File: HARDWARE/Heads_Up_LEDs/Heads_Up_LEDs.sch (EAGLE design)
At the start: 4 parts, among them J1 AUDIO_JACK_TRRSSMD_RA

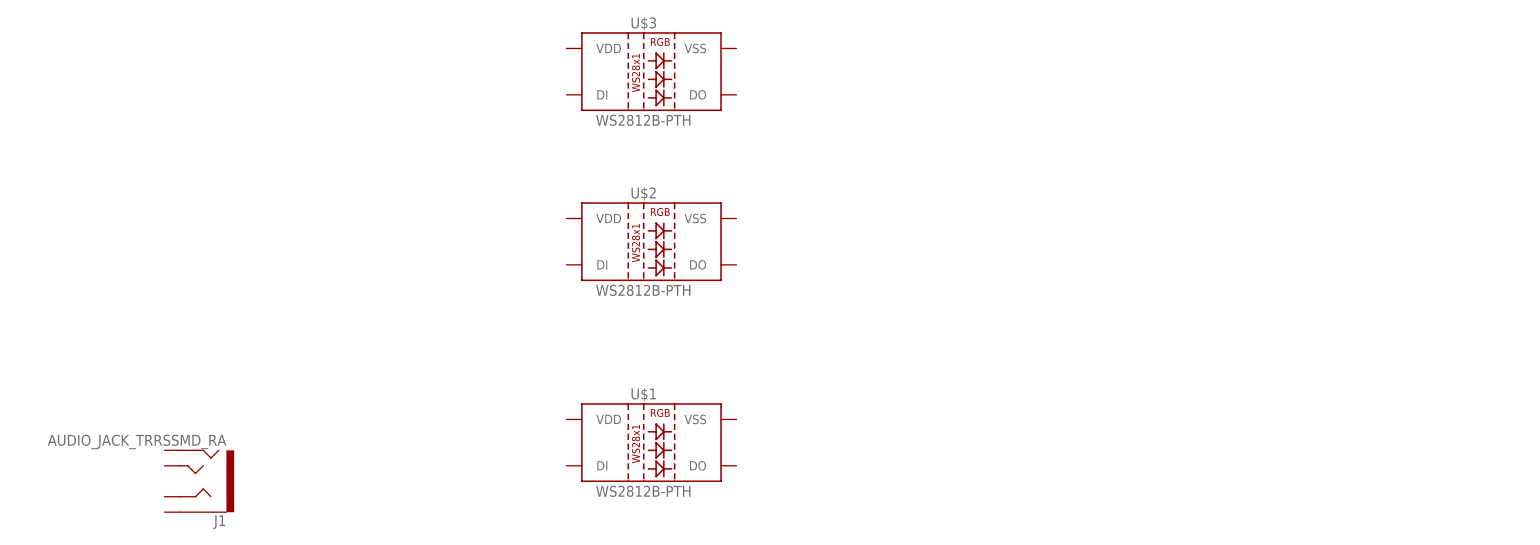
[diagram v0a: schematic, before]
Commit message: heads up leds with ws2812s - v01
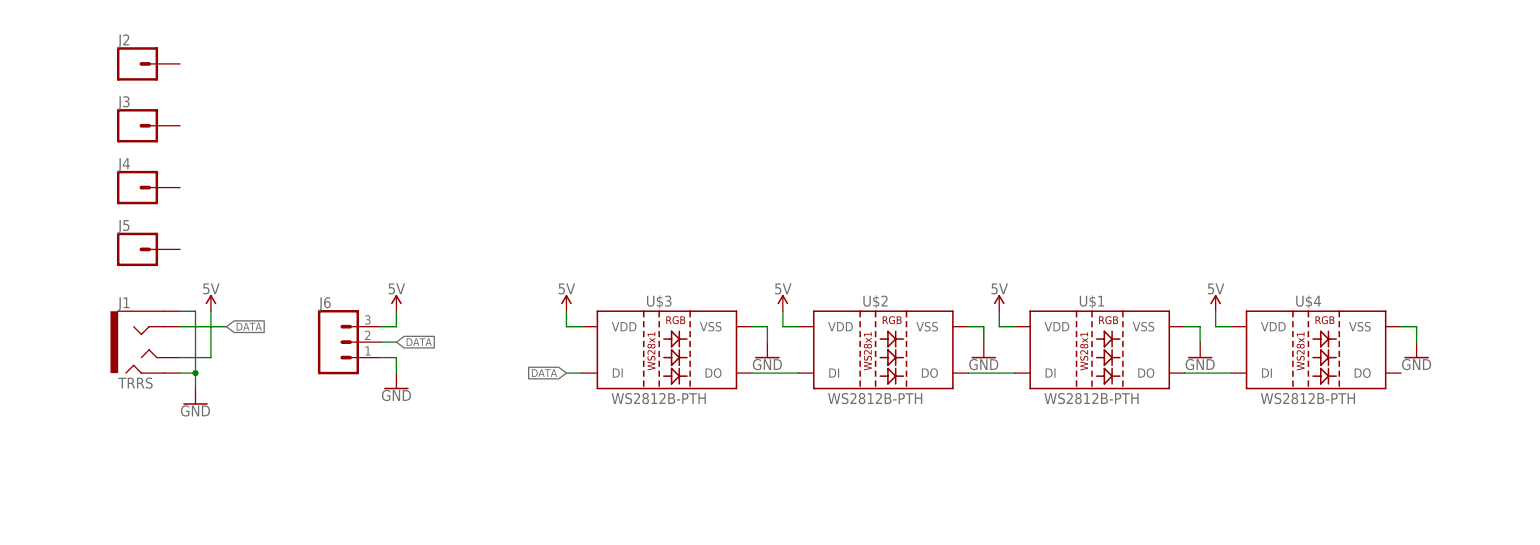
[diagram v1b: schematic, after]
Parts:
- added J2, J3, J4, J5: (no value), SparkFun-Connectors:CONN_01OFFSET
- added J6: (no value), SparkFun-Connectors:CONN_03
- added U$4: WS2812B-PTH, SparkFun-LED:WS2812B-PTH
- J1: value AUDIO_JACK_TRRSSMD_RA -> TRRS
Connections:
- new net 5V: J1.TIP, J6.3, U$1.VDD, U$2.VDD, U$3.VDD, U$4.VDD
- new net DATA: J1.RING1, J6.2, U$3.DI
- new net GND: J1.EARTH, J1.RING2, J6.1, U$1.VSS, U$2.VSS, U$3.VSS, U$4.VSS
- new net N$1: U$1.DO, U$4.DI
- new net N$7: U$2.DI, U$3.DO
- new net N$8: U$1.DI, U$2.DO
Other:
- moved on the sheet: J1, U$1, U$2, U$3
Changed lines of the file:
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@@
 </classes>
 <parts>
-<part name="J1" library="SparkFun-Connectors" deviceset="AUDIO_JACK_TRRS" device="SMD_RA"/>
+<part name="J1" library="SparkFun-Connectors" deviceset="AUDIO_JACK_TRRS" device="SMD_RA" value="TRRS"/>
 <part name="U$1" library="SparkFun-LED" deviceset="WS2812B-PTH" device=""/>
 <part name="U$2" library="SparkFun-LED" deviceset="WS2812B-PTH" device=""/>
 <part name="U$3" library="SparkFun-LED" deviceset="WS2812B-PTH" device=""/>
+<part name="J2" library="SparkFun-Connectors" deviceset="CONN_01" device="OFFSET"/>
+<part name="J3" library="SparkFun-Connectors" deviceset="CONN_01" device="OFFSET"/>
+<part name="J4" library="SparkFun-Connectors" deviceset="CONN_01" device="OFFSET"/>
+<part name="J5" library="SparkFun-Connectors" deviceset="CONN_01" device="OFFSET"/>
+<part name="J6" library="SparkFun-Connectors" deviceset="CONN_03" device=""/>
+<part name="SUPPLY1" library="SparkFun-PowerSymbols" deviceset="5V" device=""/>
+<part name="SUPPLY2" library="SparkFun-PowerSymbols" deviceset="5V" device=""/>
+<part name="SUPPLY3" library="SparkFun-PowerSymbols" deviceset="5V" device=""/>
+<part name="SUPPLY4" library="SparkFun-PowerSymbols" deviceset="5V" device=""/>
+<part name="GND1" library="SparkFun-PowerSymbols" deviceset="GND" device=""/>
+<part name="GND2" library="SparkFun-PowerSymbols" deviceset="GND" device=""/>
+<part name="GND3" library="SparkFun-PowerSymbols" deviceset="GND" device=""/>
+<part name="GND4" library="SparkFun-PowerSymbols" deviceset="GND" device=""/>
+<part name="GND5" library="SparkFun-PowerSymbols" deviceset="GND" device=""/>
+<part name="SUPPLY5" library="SparkFun-PowerSymbols" deviceset="5V" device=""/>
+<part name="U$4" library="SparkFun-LED" deviceset="WS2812B-PTH" device=""/>
+<part name="SUPPLY6" library="SparkFun-PowerSymbols" deviceset="5V" device=""/>
+<part name="GND6" library="SparkFun-PowerSymbols" deviceset="GND" device=""/>
 </parts>
 <sheets>
@@
 </plain>
 <instances>
-<instance part="J1" gate="G$1" x="48.26" y="33.02" rot="R180"/>
-<instance part="U$1" gate="G$1" x="124.46" y="38.1"/>
-<instance part="U$2" gate="G$1" x="124.46" y="71.12"/>
-<instance part="U$3" gate="G$1" x="124.46" y="99.06"/>
+<instance part="J1" gate="G$1" x="40.64" y="55.88"/>
+<instance part="U$1" gate="G$1" x="198.12" y="53.34"/>
+<instance part="U$2" gate="G$1" x="162.56" y="53.34"/>
+<instance part="U$3" gate="G$1" x="127" y="53.34"/>
+<instance part="J2" gate="G$1" x="38.1" y="101.6"/>
+<instance part="J3" gate="G$1" x="38.1" y="91.44"/>
+<instance part="J4" gate="G$1" x="38.1" y="81.28"/>
+<instance part="J5" gate="G$1" x="38.1" y="71.12"/>
+<instance part="J6" gate="J$1" x="71.12" y="55.88"/>
+<instance part="SUPPLY1" gate="G$1" x="109.22" y="60.96"/>
+<instance part="SUPPLY2" gate="G$1" x="144.78" y="60.96"/>
+<instance part="SUPPLY3" gate="G$1" x="180.34" y="60.96"/>
+<instance part="SUPPLY4" gate="G$1" x="50.8" y="60.96"/>
+<instance part="GND1" gate="1" x="48.26" y="45.72"/>
+<instance part="GND2" gate="1" x="142.24" y="53.34"/>
+<instance part="GND3" gate="1" x="177.8" y="53.34"/>
+<instance part="GND4" gate="1" x="213.36" y="53.34"/>
+<instance part="GND5" gate="1" x="81.28" y="48.26"/>
+<instance part="SUPPLY5" gate="G$1" x="81.28" y="60.96"/>
+<instance part="U$4" gate="G$1" x="233.68" y="53.34"/>
+<instance part="SUPPLY6" gate="G$1" x="215.9" y="60.96"/>
+<instance part="GND6" gate="1" x="248.92" y="53.34"/>
 </instances>
 <busses>
 </busses>
 <nets>
+<net name="N$7" class="0">
+<segment>
+<pinref part="U$3" gate="G$1" pin="DO"/>
+<pinref part="U$2" gate="G$1" pin="DI"/>
+<wire x1="139.7" y1="50.8" x2="147.32" y2="50.8" width="0.1524" layer="91"/>
+</segment>
+</net>
+<net name="N$8" class="0">
+<segment>
+<pinref part="U$2" gate="G$1" pin="DO"/>
+<pinref part="U$1" gate="G$1" pin="DI"/>
+<wire x1="175.26" y1="50.8" x2="182.88" y2="50.8" width="0.1524" layer="91"/>
+</segment>
+</net>
+<net name="5V" class="0">
+<segment>
+<pinref part="U$3" gate="G$1" pin="VDD"/>
+<wire x1="111.76" y1="58.42" x2="109.22" y2="58.42" width="0.1524" layer="91"/>
+<wire x1="109.22" y1="58.42" x2="109.22" y2="60.96" width="0.1524" layer="91"/>
+<pinref part="SUPPLY1" gate="G$1" pin="5V"/>
+</segment>
+<segment>
+<pinref part="U$2" gate="G$1" pin="VDD"/>
+<wire x1="147.32" y1="58.42" x2="144.78" y2="58.42" width="0.1524" layer="91"/>
+<wire x1="144.78" y1="58.42" x2="144.78" y2="60.96" width="0.1524" layer="91"/>
+<pinref part="SUPPLY2" gate="G$1" pin="5V"/>
+</segment>
+<segment>
+<pinref part="U$1" gate="G$1" pin="VDD"/>
+<wire x1="182.88" y1="58.42" x2="180.34" y2="58.42" width="0.1524" layer="91"/>
+<wire x1="180.34" y1="58.42" x2="180.34" y2="60.96" width="0.1524" layer="91"/>
+<pinref part="SUPPLY3" gate="G$1" pin="5V"/>
+</segment>
+<segment>
+<pinref part="SUPPLY4" gate="G$1" pin="5V"/>
+<wire x1="50.8" y1="58.42" x2="50.8" y2="60.96" width="0.1524" layer="91"/>
+<wire x1="50.8" y1="58.42" x2="50.8" y2="53.34" width="0.1524" layer="91"/>
+<pinref part="J1" gate="G$1" pin="TIP"/>
+<wire x1="50.8" y1="53.34" x2="45.72" y2="53.34" width="0.1524" layer="91"/>
+</segment>
+<segment>
+<pinref part="J6" gate="J$1" pin="3"/>
+<wire x1="78.74" y1="58.42" x2="81.28" y2="58.42" width="0.1524" layer="91"/>
+<pinref part="SUPPLY5" gate="G$1" pin="5V"/>
+<wire x1="81.28" y1="58.42" x2="81.28" y2="60.96" width="0.1524" layer="91"/>
+</segment>
+<segment>
+<pinref part="U$4" gate="G$1" pin="VDD"/>
+<wire x1="218.44" y1="58.42" x2="215.9" y2="58.42" width="0.1524" layer="91"/>
+<wire x1="215.9" y1="58.42" x2="215.9" y2="60.96" width="0.1524" layer="91"/>
+<pinref part="SUPPLY6" gate="G$1" pin="5V"/>
+</segment>
+</net>
+<net name="GND" class="0">
+<segment>
+<pinref part="U$3" gate="G$1" pin="VSS"/>
+<wire x1="139.7" y1="58.42" x2="142.24" y2="58.42" width="0.1524" layer="91"/>
+<wire x1="142.24" y1="58.42" x2="142.24" y2="55.88" width="0.1524" layer="91"/>
+<pinref part="GND2" gate="1" pin="GND"/>
+</segment>
+<segment>
+<pinref part="U$2" gate="G$1" pin="VSS"/>
+<wire x1="175.26" y1="58.42" x2="177.8" y2="58.42" width="0.1524" layer="91"/>
+<wire x1="177.8" y1="58.42" x2="177.8" y2="55.88" width="0.1524" layer="91"/>
+<pinref part="GND3" gate="1" pin="GND"/>
+</segment>
+<segment>
+<pinref part="U$1" gate="G$1" pin="VSS"/>
+<wire x1="210.82" y1="58.42" x2="213.36" y2="58.42" width="0.1524" layer="91"/>
+<wire x1="213.36" y1="58.42" x2="213.36" y2="55.88" width="0.1524" layer="91"/>
+<pinref part="GND4" gate="1" pin="GND"/>
+</segment>
+<segment>
+<pinref part="J1" gate="G$1" pin="EARTH"/>
+<wire x1="45.72" y1="60.96" x2="48.26" y2="60.96" width="0.1524" layer="91"/>
+<wire x1="48.26" y1="60.96" x2="48.26" y2="50.8" width="0.1524" layer="91"/>
+<pinref part="J1" gate="G$1" pin="RING2"/>
+<wire x1="48.26" y1="50.8" x2="48.26" y2="48.26" width="0.1524" layer="91"/>
+<wire x1="45.72" y1="50.8" x2="48.26" y2="50.8" width="0.1524" layer="91"/>
+<junction x="48.26" y="50.8"/>
+<pinref part="GND1" gate="1" pin="GND"/>
+</segment>
+<segment>
+<pinref part="J6" gate="J$1" pin="1"/>
+<wire x1="78.74" y1="53.34" x2="81.28" y2="53.34" width="0.1524" layer="91"/>
+<pinref part="GND5" gate="1" pin="GND"/>
+<wire x1="81.28" y1="53.34" x2="81.28" y2="50.8" width="0.1524" layer="91"/>
+</segment>
+<segment>
+<pinref part="U$4" gate="G$1" pin="VSS"/>
+<wire x1="246.38" y1="58.42" x2="248.92" y2="58.42" width="0.1524" layer="91"/>
+<wire x1="248.92" y1="58.42" x2="248.92" y2="55.88" width="0.1524" layer="91"/>
+<pinref part="GND6" gate="1" pin="GND"/>
+</segment>
+</net>
+<net name="DATA" class="0">
+<segment>
+<pinref part="U$3" gate="G$1" pin="DI"/>
+<wire x1="111.76" y1="50.8" x2="109.22" y2="50.8" width="0.1524" layer="91"/>
+<label x="109.22" y="50.8" size="1.27" layer="95" rot="R180" xref="yes"/>
+</segment>
+<segment>
+<pinref part="J6" gate="J$1" pin="2"/>
+<wire x1="78.74" y1="55.88" x2="81.28" y2="55.88" width="0.1524" layer="91"/>
+<label x="81.28" y="55.88" size="1.27" layer="95" xref="yes"/>
+</segment>
+<segment>
+<pinref part="J1" gate="G$1" pin="RING1"/>
+<wire x1="45.72" y1="58.42" x2="53.34" y2="58.42" width="0.1524" layer="91"/>
+<label x="53.34" y="58.42" size="1.27" layer="95" xref="yes"/>
+</segment>
+</net>
+<net name="N$1" class="0">
+<segment>
+<pinref part="U$1" gate="G$1" pin="DO"/>
+<pinref part="U$4" gate="G$1" pin="DI"/>
+<wire x1="210.82" y1="50.8" x2="218.44" y2="50.8" width="0.1524" layer="91"/>
+</segment>
+</net>
 </nets>
 </sheet>
